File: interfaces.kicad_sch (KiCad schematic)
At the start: 36 parts, among them J4 1140084168, J5 0473460001, U1 TS3USB30EDGSR, U5 TS3USB30EDGSR, U6 FT234XD-R

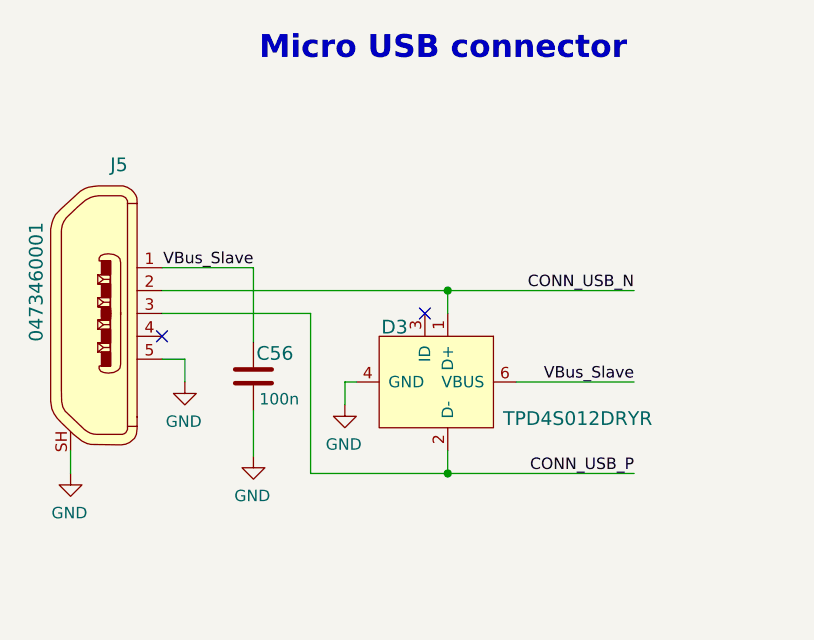
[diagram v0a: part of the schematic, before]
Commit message: Update DF40HC(3.0)-100DS-0.4v symbol and footprint
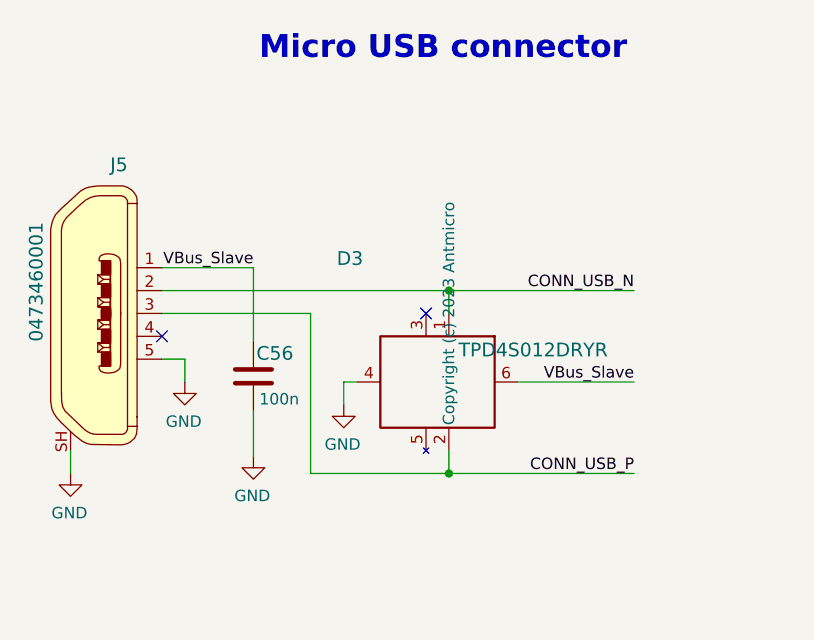
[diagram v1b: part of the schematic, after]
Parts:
- D3: footprint scalenode-cm4-baseboard-footprints:UFDFN-6_1.45x1mm -> antmicro-footprints:UFDFN-6_1.45x1mm; symbol scalenode-cm4-baseboard:TPD4S012DRYR -> antmicroTVSDiodes:TPD4S012DRYR; Author (none) -> Antmicro; Copyright (none) -> Copyright (c) 2023 Antmicro; License (none) -> Apache-2.0
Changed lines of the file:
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@@
   (junction (at 48.006 183.896) (diameter 0) (color 0 0 0 0)
   )
-  (junction (at 79.629 63.5) (diameter 0) (color 0 0 0 0)
-  )
   (junction (at 244.094 104.394) (diameter 0) (color 0 0 0 0)
   )
@@
   (junction (at 111.506 205.486) (diameter 0) (color 0 0 0 0)
   )
+  (junction (at 79.756 63.5) (diameter 0) (color 0 0 0 0)
+  )
   (junction (at 321.564 47.244) (diameter 0) (color 0 0 0 0)
   )
@@
   (junction (at 89.916 159.766) (diameter 0) (color 0 0 0 0)
   )
-  (junction (at 79.629 83.82) (diameter 0) (color 0 0 0 0)
-  )
   (junction (at 84.836 159.766) (diameter 0) (color 0 0 0 0)
   )
   (junction (at 325.374 57.404) (diameter 0) (color 0 0 0 0)
   )
+  (junction (at 79.756 83.82) (diameter 0) (color 0 0 0 0)
+  )
   (junction (at 324.104 104.394) (diameter 0) (color 0 0 0 0)
   )
@@
   (no_connect (at 266.192 197.866))
   (no_connect (at 289.052 192.786))
-  (no_connect (at 77.089 66.04))
+  (no_connect (at 77.216 66.04))
   (no_connect (at 47.879 68.58))
   (wire (pts (xy 47.879 71.12) (xy 50.419 71.12))
@@
     (stroke (width 0) (type default) (color 0 0 0 0))
   )
-  (wire (pts (xy 100.33 63.5) (xy 79.629 63.5))
-    (stroke (width 0) (type default) (color 0 0 0 0))
-  )
   (wire (pts (xy 329.184 57.404) (xy 325.374 57.404))
     (stroke (width 0) (type default) (color 0 0 0 0))
@@
     (stroke (width 0) (type default) (color 0 0 0 0))
   )
-  (wire (pts (xy 69.469 73.66) (xy 68.199 73.66))
-    (stroke (width 0) (type default) (color 0 0 0 0))
-  )
   (wire (pts (xy 293.624 187.706) (xy 289.052 187.706))
     (stroke (width 0) (type default) (color 0 0 0 0))
@@
     (stroke (width 0) (type default) (color 0 0 0 0))
   )
-  (wire (pts (xy 79.629 63.5) (xy 47.879 63.5))
-    (stroke (width 0) (type default) (color 0 0 0 0))
-  )
   (wire (pts (xy 216.154 55.88) (xy 216.154 57.15))
     (stroke (width 0) (type default) (color 0 0 0 0))
@@
     (stroke (width 0) (type default) (color 0 0 0 0))
   )
-  (wire (pts (xy 100.33 73.66) (xy 87.249 73.66))
-    (stroke (width 0) (type default) (color 0 0 0 0))
-  )
   (wire (pts (xy 37.846 183.896) (xy 48.006 183.896))
     (stroke (width 0) (type default) (color 0 0 0 0))
@@
     (stroke (width 0) (type default) (color 0 0 0 0))
   )
-  (wire (pts (xy 100.33 83.82) (xy 79.629 83.82))
-    (stroke (width 0) (type default) (color 0 0 0 0))
-  )
   (wire (pts (xy 149.479 56.388) (xy 146.304 56.388))
     (stroke (width 0) (type default) (color 0 0 0 0))
@@
     (stroke (width 0) (type default) (color 0 0 0 0))
   )
-  (wire (pts (xy 68.199 73.66) (xy 68.199 76.2))
-    (stroke (width 0) (type default) (color 0 0 0 0))
-  )
   (wire (pts (xy 219.964 57.15) (xy 223.774 57.15))
     (stroke (width 0) (type default) (color 0 0 0 0))
@@
     (stroke (width 0) (type default) (color 0 0 0 0))
   )
-  (wire (pts (xy 79.629 83.82) (xy 64.389 83.82))
+  (wire (pts (xy 64.389 83.82) (xy 79.756 83.82))
     (stroke (width 0) (type default) (color 0 0 0 0))
   )
@@
     (stroke (width 0) (type default) (color 0 0 0 0))
   )
-  (wire (pts (xy 79.629 81.28) (xy 79.629 83.82))
-    (stroke (width 0) (type default) (color 0 0 0 0))
-  )
   (wire (pts (xy 136.144 53.848) (xy 122.682 53.848))
     (stroke (width 0) (type default) (color 0 0 0 0))
@@
     (stroke (width 0) (type default) (color 0 0 0 0))
   )
+  (wire (pts (xy 68.072 73.66) (xy 69.596 73.66))
+    (stroke (width 0) (type default) (color 0 0 0 0))
+  )
   (wire (pts (xy 45.466 171.196) (xy 45.466 188.976))
     (stroke (width 0) (type default) (color 0 0 0 0))
@@
     (stroke (width 0) (type default) (color 0 0 0 0))
   )
+  (wire (pts (xy 79.756 81.28) (xy 79.756 83.82))
+    (stroke (width 0) (type default) (color 0 0 0 0))
+  )
   (wire (pts (xy 58.039 60.96) (xy 58.039 69.215))
     (stroke (width 0) (type default) (color 0 0 0 0))
   )
+  (wire (pts (xy 79.756 83.82) (xy 100.33 83.82))
+    (stroke (width 0) (type default) (color 0 0 0 0))
+  )
   (wire (pts (xy 307.34 67.564) (xy 325.374 67.564))
     (stroke (width 0) (type default) (color 0 0 0 0))
@@
     (stroke (width 0) (type default) (color 0 0 0 0))
   )
-  (wire (pts (xy 79.629 66.04) (xy 79.629 63.5))
+  (wire (pts (xy 47.879 63.5) (xy 79.756 63.5))
     (stroke (width 0) (type default) (color 0 0 0 0))
   )
@@
     (stroke (width 0) (type default) (color 0 0 0 0))
   )
+  (wire (pts (xy 79.756 63.5) (xy 100.33 63.5))
+    (stroke (width 0) (type default) (color 0 0 0 0))
+  )
+  (wire (pts (xy 79.756 63.5) (xy 79.756 66.04))
+    (stroke (width 0) (type default) (color 0 0 0 0))
+  )
   (wire (pts (xy 325.374 82.804) (xy 242.824 82.804))
     (stroke (width 0) (type default) (color 0 0 0 0))
@@
     (stroke (width 0) (type default) (color 0 0 0 0))
   )
+  (wire (pts (xy 68.072 73.66) (xy 68.072 76.2))
+    (stroke (width 0) (type default) (color 0 0 0 0))
+  )
   (wire (pts (xy 225.044 70.104) (xy 211.709 70.104))
     (stroke (width 0) (type default) (color 0 0 0 0))
@@
     (stroke (width 0) (type default) (color 0 0 0 0))
   )
+  (wire (pts (xy 87.376 73.66) (xy 100.33 73.66))
+    (stroke (width 0) (type default) (color 0 0 0 0))
+  )
   (wire (pts (xy 89.916 169.926) (xy 89.916 176.276))
     (stroke (width 0) (type default) (color 0 0 0 0))
@@
     (pin "SH")
   )
-  (symbol (lib_id "scalenode-cm4-baseboard:GND") (at 68.199 76.2 0) (mirror y) (unit 1)
+  (symbol (lib_id "scalenode-cm4-baseboard:GND") (at 68.072 76.2 0) (mirror y) (unit 1)
     (in_bom yes) (on_board yes)
-    (property "Reference" "#PWR014" (id 0) (at 68.199 82.55 0)
+    (property "Reference" "#PWR014" (id 0) (at 68.072 82.55 0)
       (effects (font (size 1.27 1.27)) hide)
     )
-    (property "Value" "GND" (id 1) (at 68.072 80.5942 0))
-    (property "Footprint" "" (id 2) (at 68.199 76.2 0)
+    (property "Value" "GND" (id 1) (at 67.945 80.5942 0))
+    (property "Footprint" "" (id 2) (at 68.072 76.2 0)
       (effects (font (size 1.27 1.27)) hide)
     )
-    (property "Datasheet" "" (id 3) (at 68.199 76.2 0)
+    (property "Datasheet" "" (id 3) (at 68.072 76.2 0)
       (effects (font (size 1.27 1.27)) hide)
     )
     (pin "1")
   )
-  (symbol (lib_id "scalenode-cm4-baseboard:TPD4S012DRYR") (at 84.709 73.66 270) (unit 1)
+  (symbol (lib_id "antmicroTVSDiodes:TPD4S012DRYR") (at 79.756 66.04 270) (unit 1)
     (in_bom yes) (on_board yes)
-    (property "Reference" "D3" (id 0) (at 75.184 67.564 90)
+    (property "Reference" "D3" (id 0) (at 70.231 59.944 90)
       (effects (font (size 1.524 1.524)) (justify right))
     )
-    (property "Value" "TPD4S012DRYR" (id 1) (at 102.362 77.724 90)
+    (property "Value" "TPD4S012DRYR" (id 1) (at 97.409 70.104 90)
       (effects (font (size 1.524 1.524)) (justify right))
     )
-    (property "Footprint" "scalenode-cm4-baseboard-footprints:UFDFN-6_1.45x1mm" (id 2) (at 89.789 78.74 0)
-      (effects (font (size 1.524 1.524)) (justify left) hide)
+    (property "Footprint" "antmicro-footprints:UFDFN-6_1.45x1mm" (id 2) (at 77.216 96.52 0)
+      (effects (font (size 1.27 1.27) (thickness 0.15)) (justify left bottom) hide)
     )
-    (property "Datasheet" "http://www.ti.com/general/docs/suppproductinfo.tsp?distId=10&gotoUrl=http%3A%2F%2Fwww.ti.com%2Flit%2Fgpn%2Ftpd4s012" (id 3) (at 92.329 78.74 0)
-      (effects (font (size 1.524 1.524)) (justify left) hide)
+    (property "Datasheet" "http://www.ti.com/general/docs/suppproductinfo.tsp?distId=10&gotoUrl=http%3A%2F%2Fwww.ti.com%2Flit%2Fgpn%2Ftpd4s012" (id 3) (at 74.676 96.52 0)
+      (effects (font (size 1.27 1.27) (thickness 0.15)) (justify left bottom) hide)
     )
-    (property "Manufacturer" "Texas Instruments" (id 4) (at 112.649 78.74 0)
-      (effects (font (size 1.524 1.524)) (justify left) hide)
+    (property "Manufacturer" "Texas Instruments" (id 4) (at 72.136 96.52 0)
+      (effects (font (size 1.27 1.27) (thickness 0.15)) (justify left bottom) hide)
     )
-    (property "MPN" "TPD4S012DRYR" (id 5) (at 97.409 78.74 0)
-      (effects (font (size 1.524 1.524)) (justify left) hide)
+    (property "MPN" "TPD4S012DRYR" (id 5) (at 69.596 96.52 0)
+      (effects (font (size 1.27 1.27) (thickness 0.15)) (justify left bottom) hide)
+    )
+    (property "Author" "Antmicro" (id 6) (at 67.056 96.52 0)
+      (effects (font (size 1.27 1.27) (thickness 0.15)) (justify left bottom) hide)
+    )
+    (property "License" "Apache-2.0" (id 7) (at 64.516 96.52 0)
+      (effects (font (size 1.27 1.27) (thickness 0.15)) (justify left bottom) hide)
     )
+    (property "Copyright" "Copyright (c) 2023 Antmicro" (id 8) (at 79.756 66.04 0))
     (pin "1")
     (pin "2")

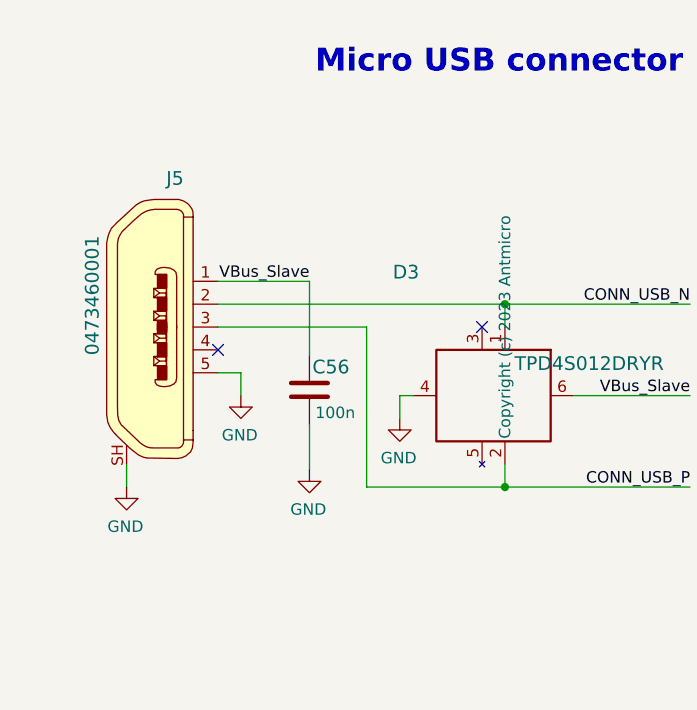
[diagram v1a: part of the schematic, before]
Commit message: Update USB_Micro_B_Female_0473460001 symbol and footprint
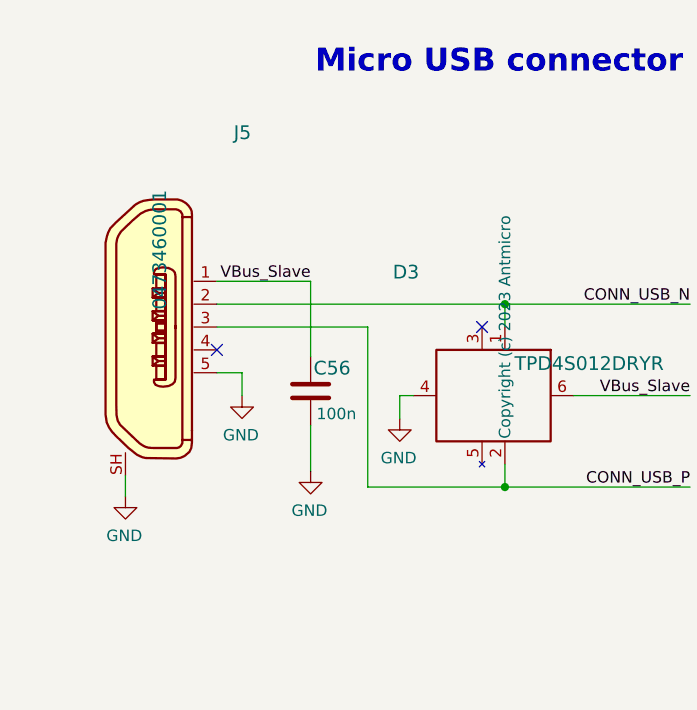
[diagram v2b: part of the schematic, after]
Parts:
- J5: footprint scalenode-cm4-baseboard-footprints:USB_Micro_B_Female_0473460001 -> antmicro-footprints:USB_Micro_B_Female_0473460001; symbol scalenode-cm4-baseboard:0473460001 -> antmicroUSBDVIHDMIConnectors:USB-Micro-B_0473460001; Author (none) -> Antmicro; Copyright (none) -> Copyright (c) 2023 Antmicro; License (none) -> Apache-2.0

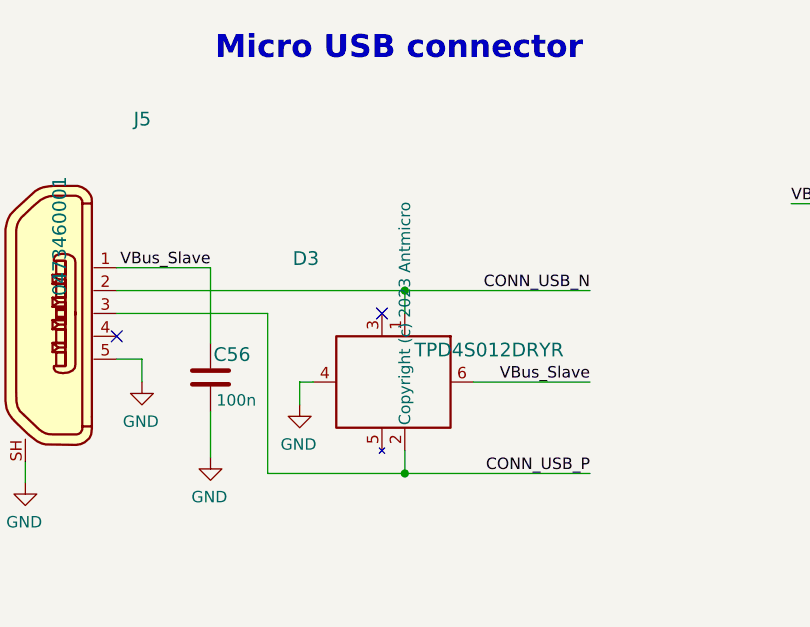
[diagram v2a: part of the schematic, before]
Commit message: Update TPD4S012DRYR symbol and footprint
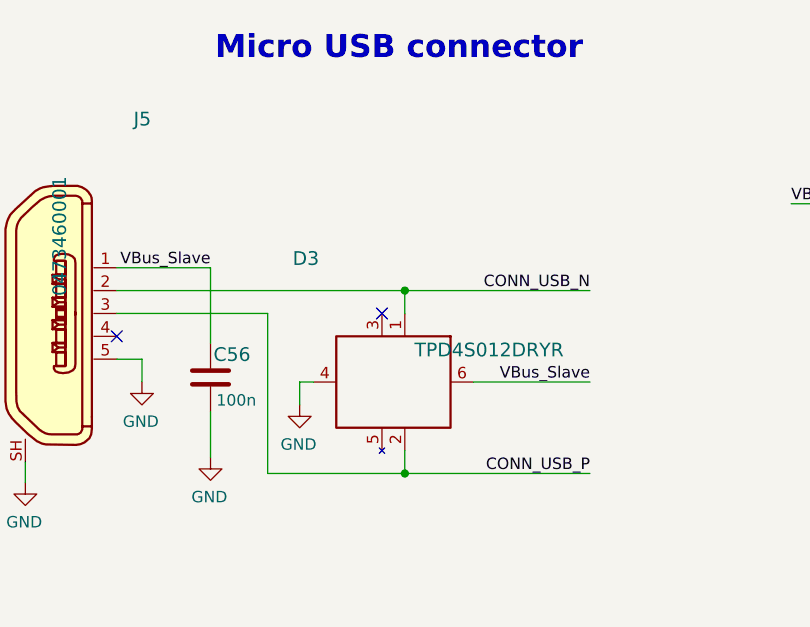
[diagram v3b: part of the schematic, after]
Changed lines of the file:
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@@
       (effects (font (size 1.27 1.27) (thickness 0.15)) (justify left bottom) hide)
     )
-    (property "Copyright" "Copyright (c) 2023 Antmicro" (id 8) (at 79.756 66.04 0))
+    (property "Copyright" "Copyright (c) 2023 Antmicro" (id 8) (at 79.756 66.04 0)
+      (effects (font (size 1.27 1.27)) hide)
+    )
     (pin "1")
     (pin "2")

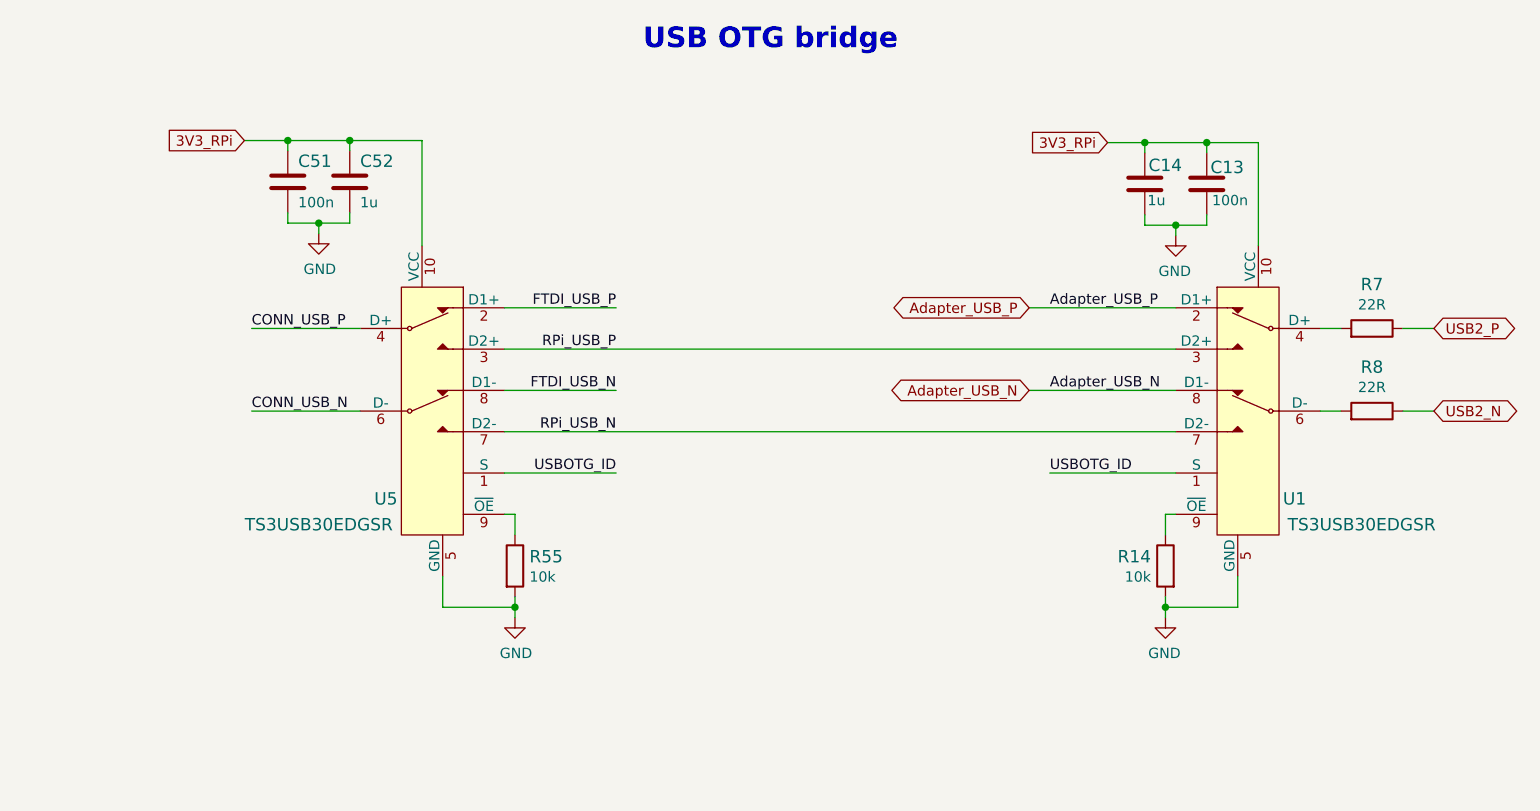
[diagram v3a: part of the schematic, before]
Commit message: Update TS3USB30EDGSR symbol and footprint
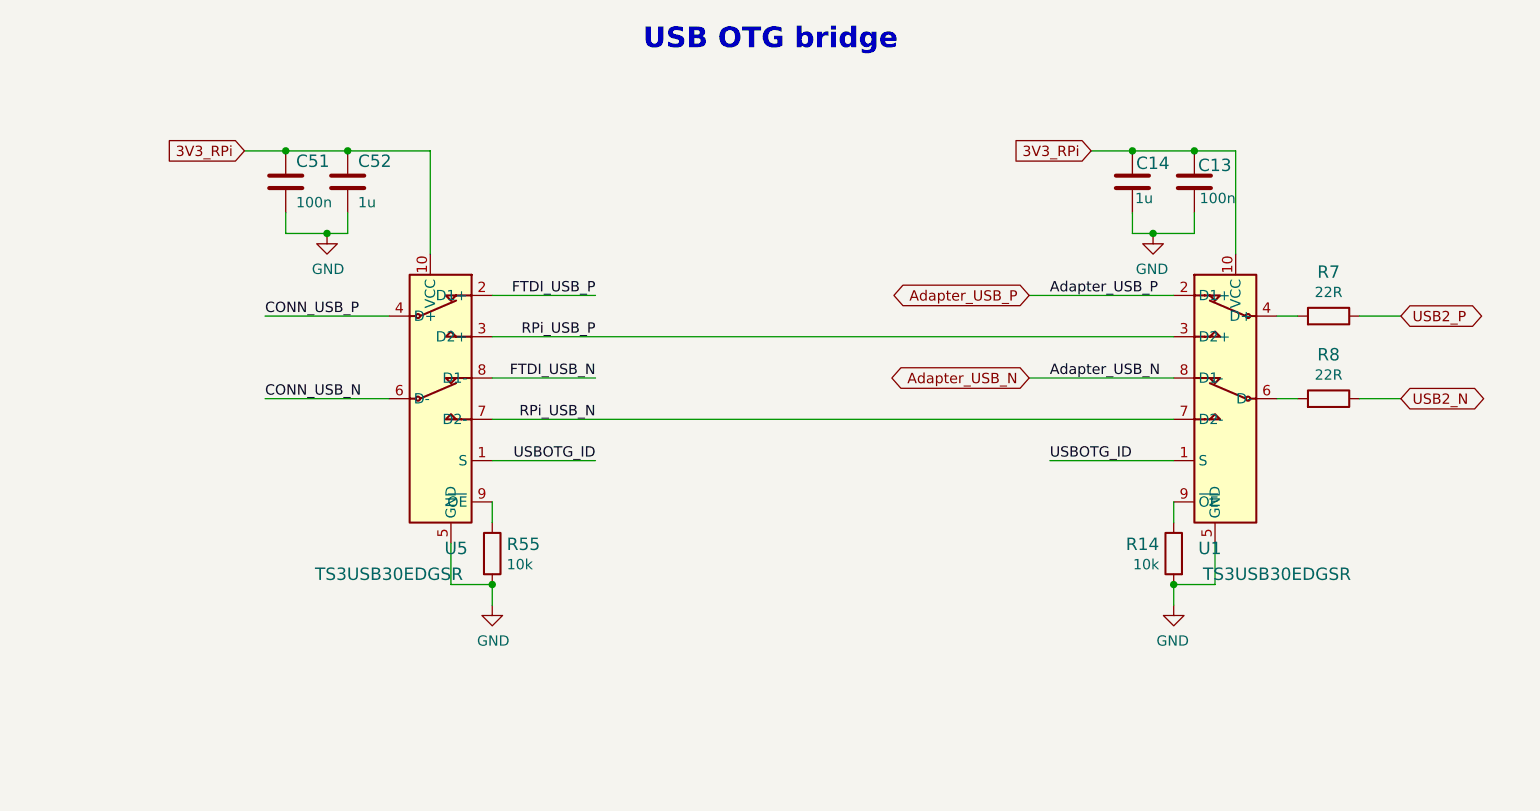
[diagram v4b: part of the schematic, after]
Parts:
- U1, U5: footprint scalenode-cm4-baseboard-footprints:MSOP-10_W3mm -> antmicro-footprints:MSOP-10_W3mm; symbol scalenode-cm4-baseboard:TS3USB30EDGSR -> antmicroInterfaceAnalogSwitchesSpecialPurpose:TS3USB30EDGSR; Author (none) -> Antmicro; Copyright (none) -> Copyright (c) 2023 Antmicro; License (none) -> Apache-2.0
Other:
- moved on the sheet: C13, C14, R14, R55, R7, R8
